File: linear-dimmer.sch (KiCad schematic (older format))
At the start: 30 parts, among them CON1 AVR-ISP-6, IC1 ATTINY85-S, P1 POWER, P2 OUTPUT, Q1 Q_NMOS_GDS, SW1 ENCODER, U1 LM78L05ACZ, U2 MCP6401

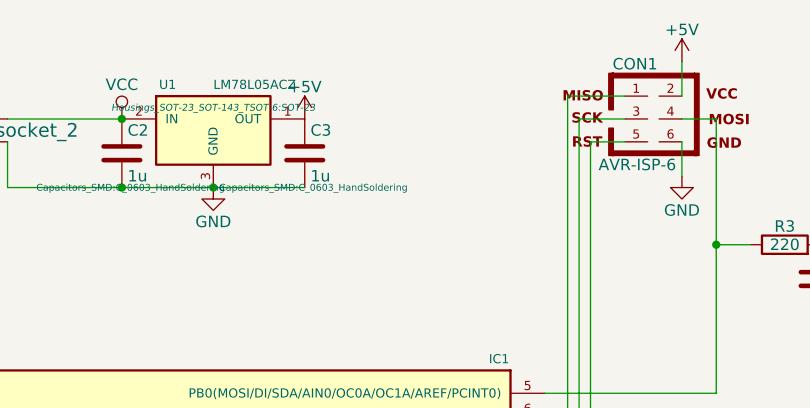
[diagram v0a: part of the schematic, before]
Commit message: Add LED, shuffle stuff around
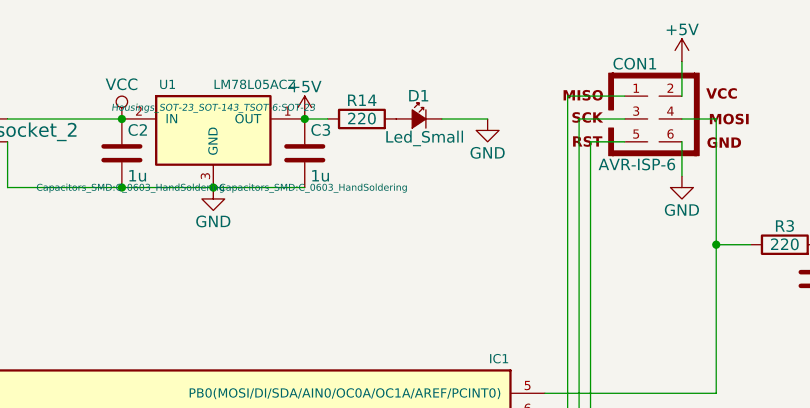
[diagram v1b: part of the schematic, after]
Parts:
- added D1: Led_Small, w_smd_leds:Led_0603, symbol Led_Small
- added R14: 220, Resistors_SMD:R_0603_HandSoldering, symbol R
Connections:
- net +5V: now also R14.1
- net GND: now also D1.2 (C)
- new net: D1.1 (A), R14.2
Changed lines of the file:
@@
 $EndComp
 $Comp
-L +5V #PWR01
+L +5V #PWR1
 U 1 1 55906375
 P 2000 3750
-F 0 "#PWR01" H 2000 3600 50  0001 C CNN
+F 0 "#PWR1" H 2000 3600 50  0001 C CNN
 F 1 "+5V" H 2000 3890 50  0000 C CNN
 F 2 "" H 2000 3750 60  0000 C CNN
@@
 $EndComp
 $Comp
-L GND #PWR02
+L GND #PWR2
 U 1 1 5590638F
 P 2000 4250
-F 0 "#PWR02" H 2000 4000 50  0001 C CNN
+F 0 "#PWR2" H 2000 4000 50  0001 C CNN
 F 1 "GND" H 2000 4100 50  0000 C CNN
 F 2 "" H 2000 4250 60  0000 C CNN
@@
 $EndComp
 $Comp
-L VCC #PWR03
+L VCC #PWR3
 U 1 1 559064AC
 P 2850 2550
-F 0 "#PWR03" H 2850 2400 50  0001 C CNN
+F 0 "#PWR3" H 2850 2400 50  0001 C CNN
 F 1 "VCC" H 2850 2700 50  0000 C CNN
 F 2 "" H 2850 2550 60  0000 C CNN
@@
 $EndComp
 $Comp
-L +5V #PWR04
+L +5V #PWR5
 U 1 1 559064FA
 P 3650 2550
-F 0 "#PWR04" H 3650 2400 50  0001 C CNN
+F 0 "#PWR5" H 3650 2400 50  0001 C CNN
 F 1 "+5V" H 3650 2690 50  0000 C CNN
 F 2 "" H 3650 2550 60  0000 C CNN
@@
 $EndComp
 $Comp
-L GND #PWR05
+L GND #PWR4
 U 1 1 5590650E
 P 3250 2850
-F 0 "#PWR05" H 3250 2600 50  0001 C CNN
+F 0 "#PWR4" H 3250 2600 50  0001 C CNN
 F 1 "GND" H 3250 2700 50  0000 C CNN
 F 2 "" H 3250 2850 60  0000 C CNN
@@
 $EndComp
 $Comp
-L GND #PWR06
+L GND #PWR7
 U 1 1 55906796
 P 4700 4850
-F 0 "#PWR06" H 4700 4600 50  0001 C CNN
+F 0 "#PWR7" H 4700 4600 50  0001 C CNN
 F 1 "GND" H 4700 4700 50  0000 C CNN
 F 2 "" H 4700 4850 60  0000 C CNN
@@
 $EndComp
 $Comp
-L +5V #PWR07
+L +5V #PWR8
 U 1 1 559067B3
 P 5100 4550
-F 0 "#PWR07" H 5100 4400 50  0001 C CNN
+F 0 "#PWR8" H 5100 4400 50  0001 C CNN
 F 1 "+5V" H 5100 4690 50  0000 C CNN
 F 2 "" H 5100 4550 60  0000 C CNN
@@
 $EndComp
 $Comp
-L GND #PWR08
+L GND #PWR14
 U 1 1 55906B52
 P 6050 3400
-F 0 "#PWR08" H 6050 3150 50  0001 C CNN
+F 0 "#PWR14" H 6050 3150 50  0001 C CNN
 F 1 "GND" H 6050 3250 50  0000 C CNN
 F 2 "" H 6050 3400 60  0000 C CNN
@@
 $EndComp
 $Comp
-L +5V #PWR09
+L +5V #PWR19
 U 1 1 55906CEE
 P 7850 3150
-F 0 "#PWR09" H 7850 3000 50  0001 C CNN
+F 0 "#PWR19" H 7850 3000 50  0001 C CNN
 F 1 "+5V" H 7850 3290 50  0000 C CNN
 F 2 "" H 7850 3150 60  0000 C CNN
@@
 $EndComp
 $Comp
-L GND #PWR010
+L GND #PWR20
 U 1 1 55906D7D
 P 7850 4250
-F 0 "#PWR010" H 7850 4000 50  0001 C CNN
+F 0 "#PWR20" H 7850 4000 50  0001 C CNN
 F 1 "GND" H 7850 4100 50  0000 C CNN
 F 2 "" H 7850 4250 60  0000 C CNN
@@
 $EndComp
 $Comp
-L GND #PWR011
+L GND #PWR22
 U 1 1 55906FE3
 P 9050 4850
-F 0 "#PWR011" H 9050 4600 50  0001 C CNN
+F 0 "#PWR22" H 9050 4600 50  0001 C CNN
 F 1 "GND" H 9050 4700 50  0000 C CNN
 F 2 "" H 9050 4850 60  0000 C CNN
@@
 $EndComp
 $Comp
-L VCC #PWR012
+L VCC #PWR21
 U 1 1 5590718D
 P 9050 3400
-F 0 "#PWR012" H 9050 3250 50  0001 C CNN
+F 0 "#PWR21" H 9050 3250 50  0001 C CNN
 F 1 "VCC" H 9050 3550 50  0000 C CNN
 F 2 "" H 9050 3400 60  0000 C CNN
@@
 $EndComp
 $Comp
-L +5V #PWR013
+L +5V #PWR15
 U 1 1 55907E74
 P 6100 4750
-F 0 "#PWR013" H 6100 4600 50  0001 C CNN
+F 0 "#PWR15" H 6100 4600 50  0001 C CNN
 F 1 "+5V" H 6100 4890 50  0000 C CNN
 F 2 "" H 6100 4750 60  0000 C CNN
@@
 $EndComp
 $Comp
-L GND #PWR014
+L GND #PWR13
 U 1 1 55907EEB
 P 5850 5950
-F 0 "#PWR014" H 5850 5700 50  0001 C CNN
+F 0 "#PWR13" H 5850 5700 50  0001 C CNN
 F 1 "GND" H 5850 5800 50  0000 C CNN
 F 2 "" H 5850 5950 60  0000 C CNN
@@
 $EndComp
 $Comp
-L +5V #PWR015
+L +5V #PWR10
 U 1 1 55908C44
 P 5300 2300
-F 0 "#PWR015" H 5300 2150 50  0001 C CNN
+F 0 "#PWR10" H 5300 2150 50  0001 C CNN
 F 1 "+5V" H 5300 2440 50  0000 C CNN
 F 2 "" H 5300 2300 60  0000 C CNN
@@
 $EndComp
 $Comp
-L GND #PWR016
+L GND #PWR11
 U 1 1 55908D86
 P 5300 2800
-F 0 "#PWR016" H 5300 2550 50  0001 C CNN
+F 0 "#PWR11" H 5300 2550 50  0001 C CNN
 F 1 "GND" H 5300 2650 50  0000 C CNN
 F 2 "" H 5300 2800 60  0000 C CNN
@@
 $EndComp
 $Comp
-L +5V #PWR017
+L +5V #PWR12
 U 1 1 5596BF06
 P 5600 4750
-F 0 "#PWR017" H 5600 4600 50  0001 C CNN
+F 0 "#PWR12" H 5600 4600 50  0001 C CNN
 F 1 "+5V" H 5600 4890 50  0000 C CNN
 F 2 "" H 5600 4750 60  0000 C CNN
@@
 $EndComp
 $Comp
-L GND #PWR018
+L GND #PWR9
 U 1 1 559A3616
 P 5100 5350
-F 0 "#PWR018" H 5100 5100 50  0001 C CNN
+F 0 "#PWR9" H 5100 5100 50  0001 C CNN
 F 1 "GND" H 5100 5200 50  0000 C CNN
 F 2 "" H 5100 5350 60  0000 C CNN
@@
 $EndComp
 $Comp
-L GND #PWR019
+L GND #PWR16
 U 1 1 559A3735
 P 6800 5050
-F 0 "#PWR019" H 6800 4800 50  0001 C CNN
+F 0 "#PWR16" H 6800 4800 50  0001 C CNN
 F 1 "GND" H 6800 4900 50  0000 C CNN
 F 2 "" H 6800 5050 60  0000 C CNN
@@
 $EndComp
 $Comp
-L GND #PWR020
+L GND #PWR18
 U 1 1 559A3DD8
 P 7600 3450
-F 0 "#PWR020" H 7600 3200 50  0001 C CNN
+F 0 "#PWR18" H 7600 3200 50  0001 C CNN
 F 1 "GND" H 7600 3300 50  0000 C CNN
 F 2 "" H 7600 3450 60  0000 C CNN
@@
 	6900 3750 7450 3750
 $Comp
-L GND #PWR021
+L GND #PWR17
 U 1 1 559D7709
 P 7100 4050
-F 0 "#PWR021" H 7100 3800 50  0001 C CNN
+F 0 "#PWR17" H 7100 3800 50  0001 C CNN
 F 1 "GND" H 7100 3900 50  0000 C CNN
 F 2 "" H 7100 4050 60  0000 C CNN
@@
 	6950 4150 6950 4550
 Connection ~ 7450 4550
+$Comp
+L R R14
+U 1 1 559D7E01
+P 3900 2550
+F 0 "R14" V 3980 2550 50  0000 C CNN
+F 1 "220" V 3900 2550 50  0000 C CNN
+F 2 "Resistors_SMD:R_0603_HandSoldering" V 3830 2550 30  0001 C CNN
+F 3 "" H 3900 2550 30  0000 C CNN
+	1    3900 2550
+	0    -1   -1   0
+$EndComp
+Wire Wire Line
+	3750 2550 3650 2550
+Connection ~ 3650 2550
+$Comp
+L Led_Small D1
+U 1 1 559D7EF2
+P 4150 2550
+F 0 "D1" H 4100 2650 50  0000 L CNN
+F 1 "Led_Small" H 4000 2470 50  0000 L CNN
+F 2 "w_smd_leds:Led_0603" V 4150 2550 60  0001 C CNN
+F 3 "" V 4150 2550 60  0000 C CNN
+	1    4150 2550
+	1    0    0    -1
+$EndComp
+$Comp
+L GND #PWR6
+U 1 1 559D7F73
+P 4450 2550
+F 0 "#PWR6" H 4450 2300 50  0001 C CNN
+F 1 "GND" H 4450 2400 50  0000 C CNN
+F 2 "" H 4450 2550 60  0000 C CNN
+F 3 "" H 4450 2550 60  0000 C CNN
+	1    4450 2550
+	1    0    0    -1
+$EndComp
+Wire Wire Line
+	4250 2550 4450 2550
 $EndSCHEMATC
